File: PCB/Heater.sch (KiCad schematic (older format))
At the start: 29 parts, among them IC1 ATTINY45-P, P1 220V 50Hz, P2 ICP, P3 DS18B20, T1 SCR

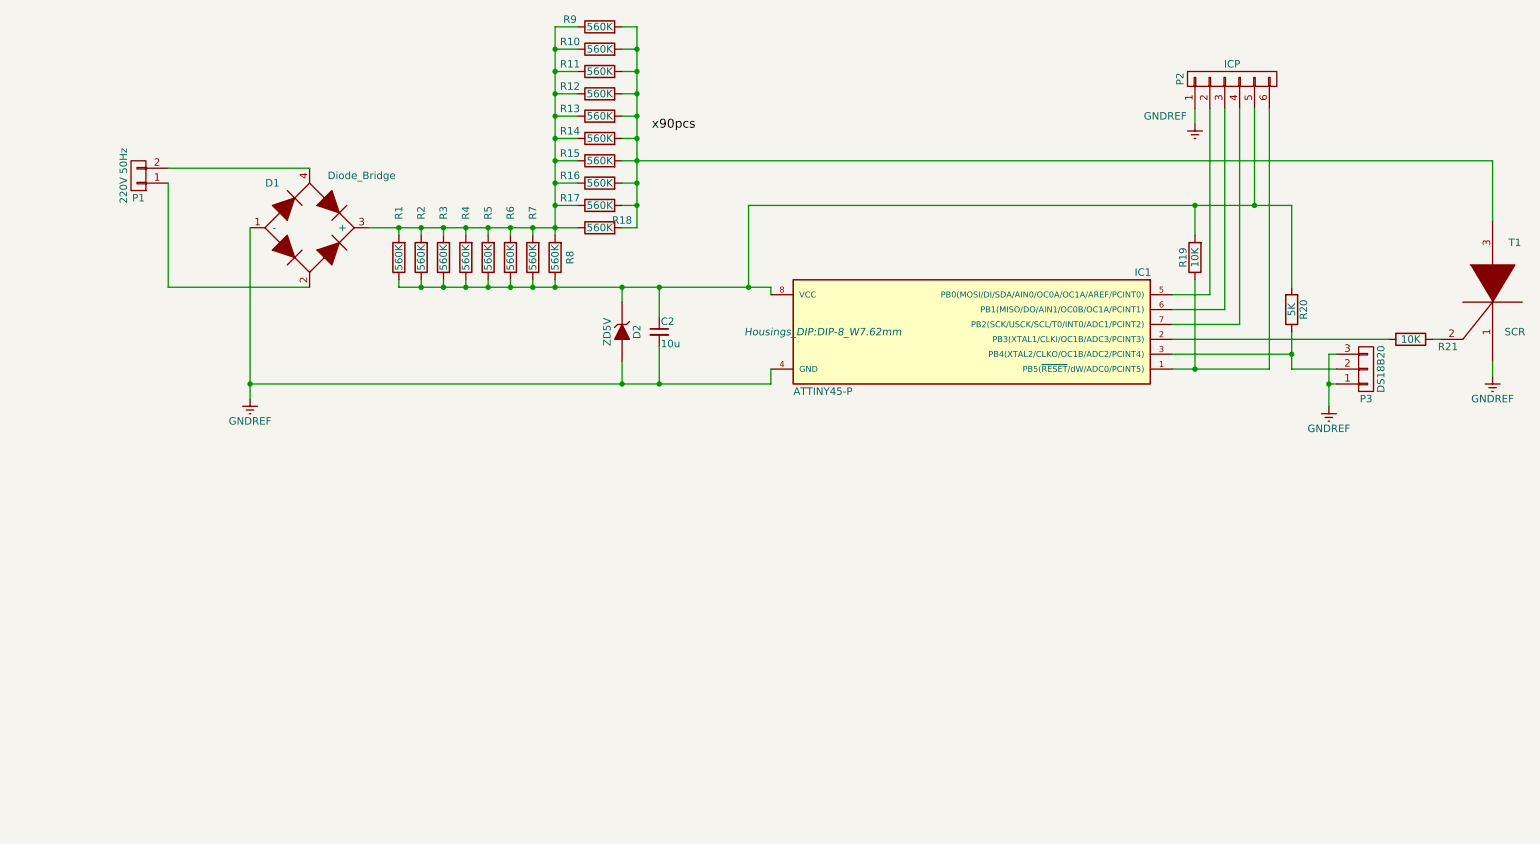
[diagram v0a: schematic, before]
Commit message: Updated Schematic and PCB to use optotriac
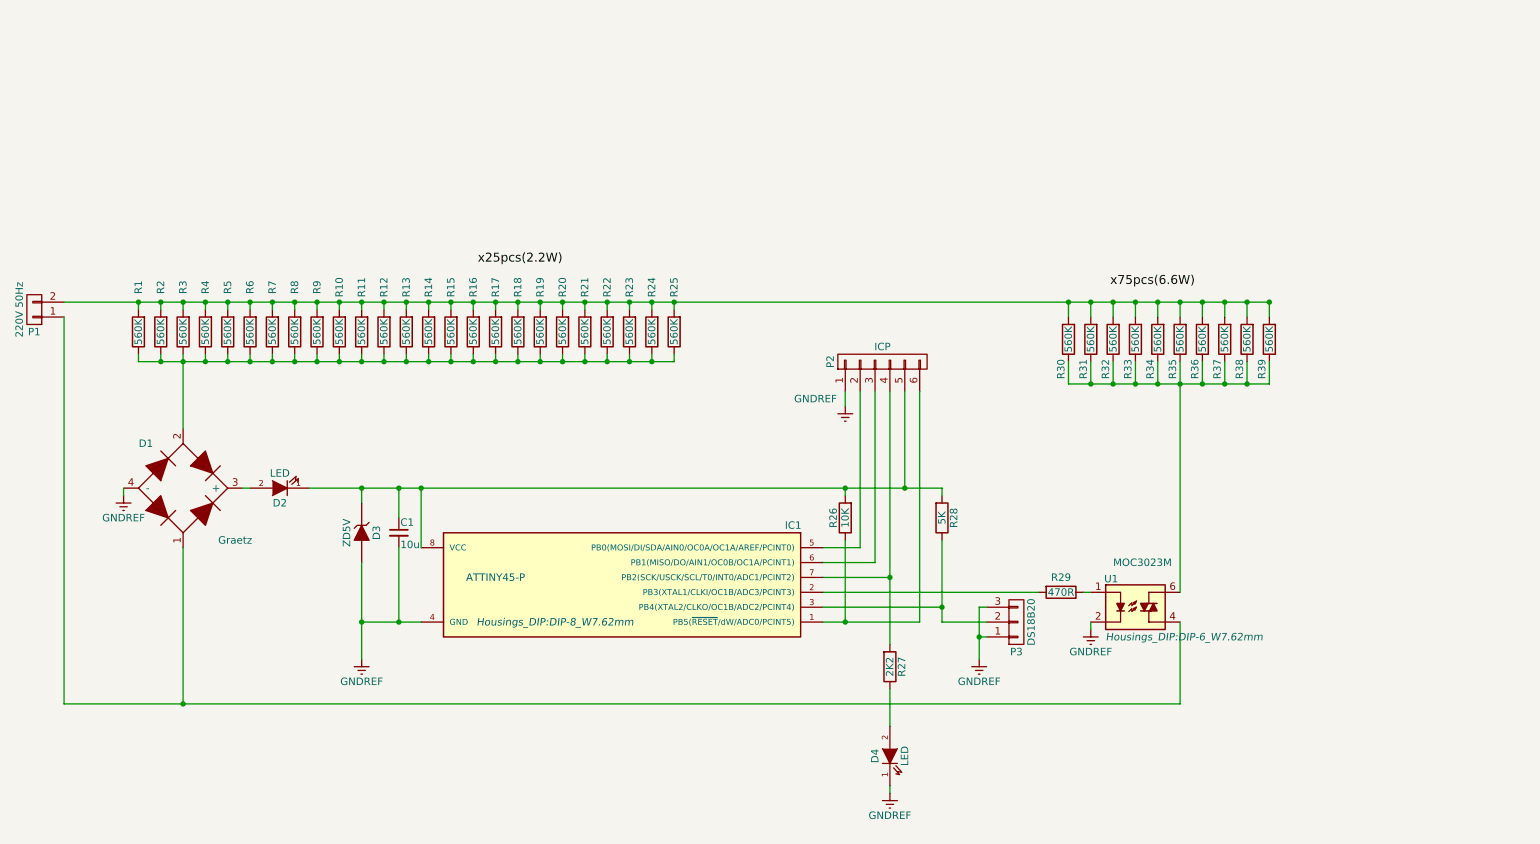
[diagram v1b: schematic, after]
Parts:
- removed D1: Diode_Bridge, Diodes_SMD:Diode_Bridge_TO-269AA, symbol Diode_Bridge
- removed T1: SCR, TO_SOT_Packages_THT:TO-92_Inline_Wide, symbol SCR
- added D1: Graetz, diodebridge:DIP-6_W7.62mm, symbol Graetz
- added D2, D4: LED, Socket_Strips:Socket_Strip_Straight_1x02_Pitch2.54mm, symbol LED
- added R10, R11, R12, R13, R14, R15, R16, R17, R18, R19, R20, R21, R22, R23, R24, R25, R9: 560K, Resistors_SMD:R_0805, symbol R
- added R27: 2K2, Resistors_SMD:R_0805, symbol R
- added U1: MOC3023M, Housings_DIP:DIP-6_W7.62mm, symbol MOC3023M
- R29: renamed from R21; value 10K -> 470R
- renumbered C2 to C1, D2 to D3, R19 to R26, R20 to R28, R9 to R30, R10 to R31, R11 to R32, R12 to R33, R13 to R34, R14 to R35, R15 to R36, R16 to R37, R17 to R38, R18 to R39
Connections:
- net GNDREF: now also D1.4 (-), D4.1 (K), U1.2
- net at IC1.7 (PB2(SCK/USCK/SCL/T0/INT0/ADC1/PCINT2)), P2.4 (P4): now also R27.2
- net at R1.1, R2.1, R3.1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: now also D1.2, R10.1, R11.1, R12.1, R13.1, R14.1, R15.1, R16.1, R17.1, R18.1, R19.1, R20.1, R21.1, R22.1, R23.1, R24.1, R25.1, R9.1; no longer C1.1, D3.1 (K), IC1.8 (VCC), P2.5 (P5), R26.2, R28.2
- net at R30.1, R31.1, R32.1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: now also U1.6; no longer R1.2, R2.2, R3.2, R4.2, R5.2, R6.2, R7.2, R8.2
- net at R29.1: now also U1.1
- net at P1.1 (P1): now also D1.1, U1.4
- net at P1.2 (P2): now also R1.2, R2.2, R3.2, R30.2, R31.2, R32.2, R33.2, R34.2, R35.2, R36.2, R37.2, R38.2, R39.2, R4.2, R5.2, R6.2, R7.2, R8.2, R10.2, R11.2, R12.2, R13.2, R14.2, R15.2, R16.2, R17.2, R18.2, R19.2, R20.2, R21.2, R22.2, R23.2, R24.2, R25.2, R9.2
- new net: C1.1, D2.1 (K), D3.1 (K), IC1.8 (VCC), P2.5 (P5), R26.2, R28.2
- new net: D1.3 (+), D2.2 (A)
- new net: D4.2 (A), R27.1
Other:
- moved on the sheet: C1, D3, IC1, P1, P2, P3, R1, R2, R26, R28, R29, R3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

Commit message: Added fw
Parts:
- D1: footprint diodebridge:DIP-6_W7.62mm -> Diodes_SMD:Diode_Bridge_TO-269AA
- D3: footprint Diodes_SMD:D_MELF -> Diodes_SMD:D_MELF_Handsoldering
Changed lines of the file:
@@
 LIBS:valves
 LIBS:diodebridge
+LIBS:Heater-cache
 EELAYER 25 0
 EELAYER END
@@
 F 0 "D3" H 3150 5150 50  0000 C CNN
 F 1 "ZD5V" H 3150 4950 50  0000 C CNN
-F 2 "Diodes_SMD:D_MELF" H 3150 5050 50  0001 C CNN
+F 2 "Diodes_SMD:D_MELF_Handsoldering" H 3150 5050 50  0001 C CNN
 F 3 "" H 3150 5050 50  0000 C CNN
 	1    3150 5050
@@
 F 0 "D1" H 1700 5050 50  0000 C CNN
 F 1 "Graetz" H 2300 4400 50  0000 C CNN
-F 2 "diodebridge:DIP-6_W7.62mm" H 1950 4750 50  0001 C CNN
+F 2 "Diodes_SMD:Diode_Bridge_TO-269AA" H 1950 4750 50  0001 C CNN
 F 3 "" H 1950 4750 50  0000 C CNN
 	1    1950 4750

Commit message: Not working yet
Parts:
- D2, D4: symbol LED -> LED-RESCUE-Heater
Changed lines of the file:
@@
 EESchema Schematic File Version 2
+LIBS:Heater-rescue
 LIBS:power
 LIBS:device
@@
 Connection ~ 1950 6200
 $Comp
-L LED D2
+L LED-RESCUE-Heater D2
 U 1 1 5961854B
 P 2600 4750
@@
 x25pcs(2.2W)
 $Comp
-L LED D4
+L LED-RESCUE-Heater D4
 U 1 1 5961C8F6
 P 6700 6550

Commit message: finished working version of the PCB and FW
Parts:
- removed P2: ICP, Socket_Strips:Socket_Strip_Straight_1x06_Pitch2.54mm, symbol CONN_01X06
- added J1: GND, Pin_Headers:Pin_Header_Straight_1x01_Pitch1.27mm, symbol CONN_01X01
- added J2: RST, Pin_Headers:Pin_Header_Straight_1x01_Pitch1.27mm, symbol CONN_01X01
- added P2: CONN_01X04, Pin_Headers:Pin_Header_Straight_1x04_Pitch2.54mm, symbol CONN_01X04
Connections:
- net GNDREF: now also J1.1 (P1)
- net at IC1.1 (PB5(~RESET~/dW/ADC0/PCINT5)), R26.1: now also J2.1 (P1)
- net at IC1.2 (PB3(XTAL1/CLKI/OC1B/ADC3/PCINT3)): now also P3.2 (P2), R28.1; no longer R29.2
- net at IC1.5 (PB0(MOSI/DI/SDA/AIN0/OC0A/OC1A/AREF/PCINT0)): now also P2.1 (P1)
- net at IC1.6 (PB1(MISO/DO/AIN1/OC0B/OC1A/PCINT1)): now also P2.2 (P2)
- net at IC1.7 (PB2(SCK/USCK/SCL/T0/INT0/ADC1/PCINT2)), R27.2: now also P2.3 (P3)
- net at C1.1, D2.1 (K), D3.1 (K)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: now also P2.4 (P4)
- net at D1.1, P1.1 (P1): now also U1.6; no longer U1.4
- net at R30.1, R31.1, R32.1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: now also U1.4; no longer U1.6
- new net: IC1.3 (PB4(XTAL2/CLKO/OC1B/ADC2/PCINT4)), R29.2
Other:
- moved on the sheet: P3, R29, U1
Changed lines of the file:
@@
 L CONN_01X03 P3
 U 1 1 595689AB
-P 7550 5650
-F 0 "P3" H 7550 5850 50  0000 C CNN
-F 1 "DS18B20" V 7650 5650 50  0000 C CNN
-F 2 "TO_SOT_Packages_THT:TO-92_Inline_Wide" H 7550 5650 50  0001 C CNN
-F 3 "" H 7550 5650 50  0000 C CNN
-	1    7550 5650
-	1    0    0    1
+P 7450 4800
+F 0 "P3" H 7450 5000 50  0000 C CNN
+F 1 "DS18B20" V 7550 4800 50  0000 C CNN
+F 2 "TO_SOT_Packages_THT:TO-92_Inline_Wide" H 7450 4800 50  0001 C CNN
+F 3 "" H 7450 4800 50  0000 C CNN
+	1    7450 4800
+	0    1    -1   0
 $EndComp
 $Comp
@@
 L R R29
 U 1 1 59568C3A
-P 7850 5450
-F 0 "R29" V 7750 5450 50  0000 C CNN
-F 1 "470R" V 7850 5450 50  0000 C CNN
-F 2 "Resistors_SMD:R_0805" V 7780 5450 50  0001 C CNN
-F 3 "" H 7850 5450 50  0000 C CNN
-	1    7850 5450
-	0    1    1    0
+P 8500 5550
+F 0 "R29" V 8400 5550 50  0000 C CNN
+F 1 "470R" V 8500 5550 50  0000 C CNN
+F 2 "Resistors_SMD:R_0805" V 8430 5550 50  0001 C CNN
+F 3 "" H 8500 5550 50  0000 C CNN
+	1    8500 5550
+	0    1    -1   0
 $EndComp
 $Comp
@@
 L GNDREF #PWR01
 U 1 1 5956A06F
-P 7300 5900
-F 0 "#PWR01" H 7300 5650 50  0001 C CNN
-F 1 "GNDREF" H 7300 5750 50  0000 C CNN
-F 2 "" H 7300 5900 50  0000 C CNN
-F 3 "" H 7300 5900 50  0000 C CNN
-	1    7300 5900
+P 7550 5150
+F 0 "#PWR01" H 7550 4900 50  0001 C CNN
+F 1 "GNDREF" H 7350 5100 50  0000 C CNN
+F 2 "" H 7550 5150 50  0000 C CNN
+F 3 "" H 7550 5150 50  0000 C CNN
+	1    7550 5150
 	-1   0    0    -1
 $EndComp
@@
 $EndComp
 $Comp
-L CONN_01X06 P2
-U 1 1 5956ABD8
-P 6650 3900
-F 0 "P2" H 6650 4250 50  0000 C CNN
-F 1 "ICP" V 6750 3900 50  0000 C CNN
-F 2 "Socket_Strips:Socket_Strip_Straight_1x06_Pitch2.54mm" H 6650 3900 50  0001 C CNN
-F 3 "" H 6650 3900 50  0000 C CNN
-	1    6650 3900
-	0    -1   -1   0
-$EndComp
-$Comp
 L R R5
 U 1 1 59576662
@@
 $Comp
 L GNDREF #PWR03
-U 1 1 5957BFE8
-P 6400 4200
-F 0 "#PWR03" H 6400 3950 50  0001 C CNN
-F 1 "GNDREF" H 6200 4250 50  0000 C CNN
-F 2 "" H 6400 4200 50  0000 C CNN
-F 3 "" H 6400 4200 50  0000 C CNN
-	1    6400 4200
-	1    0    0    -1
-$EndComp
-$Comp
-L GNDREF #PWR04
 U 1 1 59613334
 P 3150 5900
-F 0 "#PWR04" H 3150 5650 50  0001 C CNN
+F 0 "#PWR03" H 3150 5650 50  0001 C CNN
 F 1 "GNDREF" H 3150 5750 50  0000 C CNN
 F 2 "" H 3150 5900 50  0000 C CNN
@@
 L MOC3023M U1
 U 1 1 59614FA8
-P 8350 5550
-F 0 "U1" H 8140 5740 50  0000 L CNN
-F 1 "MOC3023M" H 8200 5850 50  0000 L CNN
-F 2 "Housings_DIP:DIP-6_W7.62mm" H 8150 5350 50  0000 L CIN
-F 3 "" H 8325 5550 50  0000 L CNN
-	1    8350 5550
-	1    0    0    -1
+P 8750 5900
+F 0 "U1" H 8540 6090 50  0000 L CNN
+F 1 "MOC3023M" H 8600 6200 50  0000 L CNN
+F 2 "Housings_DIP:DIP-6_W7.62mm" H 8550 5700 50  0000 L CIN
+F 3 "" H 8725 5900 50  0000 L CNN
+	1    8750 5900
+	0    -1   1    0
 $EndComp
 Connection ~ 2700 3900
@@
 Wire Wire Line
 	6250 5650 6900 5650
-Wire Wire Line
-	6250 5450 7700 5450
 Wire Wire Line
 	1650 3550 1650 3500
@@
 	3400 4950 3400 4750
 Connection ~ 3400 4750
-Wire Wire Line
-	8000 5450 8050 5450
 Connection ~ 6400 5650
 Wire Wire Line
@@
 	8800 3900 8800 4050
 Connection ~ 8800 4050
-Wire Wire Line
-	8650 3900 8650 5450
 Connection ~ 8650 4050
 Wire Wire Line
@@
 Wire Wire Line
 	9250 3500 9250 3600
-Wire Wire Line
-	6400 4200 6400 4100
 Connection ~ 6400 4750
 Connection ~ 6800 4750
 Wire Wire Line
-	6250 5550 7050 5550
-Wire Wire Line
-	7050 5100 7050 5650
-Wire Wire Line
-	7050 5650 7350 5650
-Wire Wire Line
-	7300 5750 7350 5750
-Wire Wire Line
-	7300 5550 7350 5550
-Connection ~ 7300 5750
-Wire Wire Line
-	7300 5550 7300 5900
-Connection ~ 7050 5550
+	7450 5000 7450 5450
+Wire Wire Line
+	7550 5000 7550 5150
+Wire Wire Line
+	7350 5050 7350 5000
+Connection ~ 7550 5050
 Wire Wire Line
 	2800 4750 7050 4750
@@
 Wire Wire Line
 	6800 4750 6800 4100
-Wire Wire Line
-	6900 5650 6900 4100
 Wire Wire Line
 	7050 4750 7050 4800
@@
 Connection ~ 3400 5650
 $Comp
-L GNDREF #PWR05
+L GNDREF #PWR04
 U 1 1 5961517B
-P 8050 5700
-F 0 "#PWR05" H 8050 5450 50  0001 C CNN
-F 1 "GNDREF" H 8050 5550 50  0000 C CNN
-F 2 "" H 8050 5700 50  0000 C CNN
-F 3 "" H 8050 5700 50  0000 C CNN
-	1    8050 5700
-	-1   0    0    -1
-$EndComp
-Wire Wire Line
-	8050 5700 8050 5650
+P 9050 5550
+F 0 "#PWR04" H 9050 5300 50  0001 C CNN
+F 1 "GNDREF" V 9100 5700 50  0000 C CNN
+F 2 "" H 9050 5550 50  0000 C CNN
+F 3 "" H 9050 5550 50  0000 C CNN
+	1    9050 5550
+	0    -1   -1   0
+$EndComp
 Wire Wire Line
 	1150 6200 8650 6200
 Wire Wire Line
-	8650 6200 8650 5650
-Wire Wire Line
-	9250 3900 9250 4050
+	9250 3900 9250 6200
 Wire Wire Line
 	9250 4050 7900 4050
@@
 $EndComp
 $Comp
-L GNDREF #PWR06
+L GNDREF #PWR05
 U 1 1 5961CE30
 P 6700 6800
-F 0 "#PWR06" H 6700 6550 50  0001 C CNN
+F 0 "#PWR05" H 6700 6550 50  0001 C CNN
 F 1 "GNDREF" H 6700 6650 50  0000 C CNN
 F 2 "" H 6700 6800 50  0000 C CNN
@@
 	1    0    0    -1
 $EndComp
+Wire Wire Line
+	7450 5450 6250 5450
+Wire Wire Line
+	7350 5050 7550 5050
+Wire Wire Line
+	7050 5100 7050 5450
+Connection ~ 7050 5450
+$Comp
+L CONN_01X04 P2
+U 1 1 59649114
+P 6650 3900
+F 0 "P2" H 6650 4150 50  0000 C CNN
+F 1 "CONN_01X04" V 6750 3900 50  0000 C CNN
+F 2 "Pin_Headers:Pin_Header_Straight_1x04_Pitch2.54mm" H 6650 3900 50  0001 C CNN
+F 3 "" H 6650 3900 50  0001 C CNN
+	1    6650 3900
+	0    -1   -1   0
+$EndComp
+$Comp
+L CONN_01X01 J2
+U 1 1 5964941A
+P 7100 5650
+F 0 "J2" H 7100 5750 50  0000 C CNN
+F 1 "RST" H 7250 5650 50  0000 C CNN
+F 2 "Pin_Headers:Pin_Header_Straight_1x01_Pitch1.27mm" H 7100 5650 50  0001 C CNN
+F 3 "" H 7100 5650 50  0001 C CNN
+	1    7100 5650
+	1    0    0    -1
+$EndComp
+$Comp
+L CONN_01X01 J1
+U 1 1 5964958B
+P 2950 5650
+F 0 "J1" H 2950 5750 50  0000 C CNN
+F 1 "GND" H 3100 5650 50  0000 C CNN
+F 2 "Pin_Headers:Pin_Header_Straight_1x01_Pitch1.27mm" H 2950 5650 50  0001 C CNN
+F 3 "" H 2950 5650 50  0001 C CNN
+	1    2950 5650
+	-1   0    0    1
+$EndComp
+Wire Wire Line
+	8650 3900 8650 4050
+Wire Wire Line
+	8650 5550 8650 5600
+Wire Wire Line
+	8350 5550 6250 5550
+Wire Wire Line
+	9050 5550 8850 5550
+Wire Wire Line
+	8850 5550 8850 5600
+Wire Wire Line
+	9250 6200 8850 6200
+Connection ~ 9250 4050
 $EndSCHEMATC

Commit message: A better packed version
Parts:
- removed D2: LED, Socket_Strips:Socket_Strip_Straight_1x02_Pitch2.54mm, symbol LED-RESCUE-Heater
- D1: footprint Diodes_SMD:Diode_Bridge_TO-269AA -> diodebridge:DIP-6_W7.62mm
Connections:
- net at P3.2 (P2), R28.1: now also IC1.7 (PB2(SCK/USCK/SCL/T0/INT0/ADC1/PCINT2)), P2.3 (P3); no longer IC1.2 (PB3(XTAL1/CLKI/OC1B/ADC3/PCINT3))
- net at IC1.5 (PB0(MOSI/DI/SDA/AIN0/OC0A/OC1A/AREF/PCINT0)), P2.1 (P1): now also R27.2
- net at C1.1, D3.1 (K), IC1.8 (VCC)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: now also D1.3 (+)
- net at R1.1, R10.1, R11.1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: now also D1.1; no longer D1.2
- net at R1.2, R10.2, R11.2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: now also P1.1 (P1); no longer P1.2 (P2)
- net at R30.1, R31.1, R32.1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: now also U1.6; no longer U1.4
- new net: D1.2, P1.2 (P2), U1.4
- no-connect marks 0 -> 1
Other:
- moved on the sheet: D4, R27, U1
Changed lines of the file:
@@
 F 3 "" H 950 3550 50  0000 C CNN
 	1    950  3550
-	-1   0    0    1
+	-1   0    0    -1
 $EndComp
 $Comp
@@
 L MOC3023M U1
 U 1 1 59614FA8
-P 8750 5900
-F 0 "U1" H 8540 6090 50  0000 L CNN
-F 1 "MOC3023M" H 8600 6200 50  0000 L CNN
-F 2 "Housings_DIP:DIP-6_W7.62mm" H 8550 5700 50  0000 L CIN
-F 3 "" H 8725 5900 50  0000 L CNN
-	1    8750 5900
-	0    -1   1    0
+P 8950 5800
+F 0 "U1" H 8740 5990 50  0000 L CNN
+F 1 "MOC3023M" H 8800 6100 50  0000 L CNN
+F 2 "Housings_DIP:DIP-6_W7.62mm" H 8750 5600 50  0000 L CIN
+F 3 "" H 8925 5800 50  0000 L CNN
+	1    8950 5800
+	1    0    0    -1
 $EndComp
 Connection ~ 2700 3900
-Wire Wire Line
-	6700 5350 6250 5350
 Wire Wire Line
 	6600 5250 6250 5250
@@
 Connection ~ 6800 4750
 Wire Wire Line
-	7450 5000 7450 5450
-Wire Wire Line
 	7550 5000 7550 5150
 Wire Wire Line
@@
 Connection ~ 7550 5050
 Wire Wire Line
-	2800 4750 7050 4750
+	2350 4750 7050 4750
 Wire Wire Line
 	1650 3850 1650 3900
@@
 	6400 5100 6400 5650
 Wire Wire Line
-	6500 5150 6500 4100
-Wire Wire Line
-	6600 4100 6600 5250
-Wire Wire Line
-	6700 4100 6700 5800
+	6500 4100 6500 5800
 Wire Wire Line
 	6800 4750 6800 4100
@@
 L GNDREF #PWR04
 U 1 1 5961517B
-P 9050 5550
-F 0 "#PWR04" H 9050 5300 50  0001 C CNN
-F 1 "GNDREF" V 9100 5700 50  0000 C CNN
-F 2 "" H 9050 5550 50  0000 C CNN
-F 3 "" H 9050 5550 50  0000 C CNN
-	1    9050 5550
-	0    -1   -1   0
-$EndComp
-Wire Wire Line
-	1150 6200 8650 6200
-Wire Wire Line
-	9250 3900 9250 6200
+P 8650 5950
+F 0 "#PWR04" H 8650 5700 50  0001 C CNN
+F 1 "GNDREF" H 8400 5900 50  0000 C CNN
+F 2 "" H 8650 5950 50  0000 C CNN
+F 3 "" H 8650 5950 50  0000 C CNN
+	1    8650 5950
+	1    0    0    -1
+$EndComp
+Wire Wire Line
+	1150 6200 9250 6200
 Wire Wire Line
 	9250 4050 7900 4050
@@
 	1950 5150 1950 6200
 Connection ~ 1950 6200
-$Comp
-L LED-RESCUE-Heater D2
-U 1 1 5961854B
-P 2600 4750
-F 0 "D2" H 2600 4850 50  0000 C CNN
-F 1 "LED" H 2600 4650 50  0000 C CNN
-F 2 "Socket_Strips:Socket_Strip_Straight_1x02_Pitch2.54mm" H 2600 4750 50  0001 C CNN
-F 3 "" H 2600 4750 50  0000 C CNN
-	1    2600 4750
-	-1   0    0    1
-$EndComp
-Wire Wire Line
-	2400 4750 2350 4750
 Wire Wire Line
 	2700 3900 2700 3850
@@
 L LED-RESCUE-Heater D4
 U 1 1 5961C8F6
-P 6700 6550
-F 0 "D4" H 6700 6650 50  0000 C CNN
-F 1 "LED" H 6700 6450 50  0000 C CNN
-F 2 "Socket_Strips:Socket_Strip_Straight_1x02_Pitch2.54mm" H 6700 6550 50  0001 C CNN
-F 3 "" H 6700 6550 50  0000 C CNN
-	1    6700 6550
+P 6500 6450
+F 0 "D4" H 6500 6550 50  0000 C CNN
+F 1 "LED" H 6500 6350 50  0000 C CNN
+F 2 "Socket_Strips:Socket_Strip_Straight_1x02_Pitch2.54mm" H 6500 6450 50  0001 C CNN
+F 3 "" H 6500 6450 50  0000 C CNN
+	1    6500 6450
 	0    -1   -1   0
 $EndComp
@@
 L GNDREF #PWR05
 U 1 1 5961CE30
-P 6700 6800
-F 0 "#PWR05" H 6700 6550 50  0001 C CNN
-F 1 "GNDREF" H 6700 6650 50  0000 C CNN
-F 2 "" H 6700 6800 50  0000 C CNN
-F 3 "" H 6700 6800 50  0000 C CNN
-	1    6700 6800
+P 6500 6700
+F 0 "#PWR05" H 6500 6450 50  0001 C CNN
+F 1 "GNDREF" H 6500 6550 50  0000 C CNN
+F 2 "" H 6500 6700 50  0000 C CNN
+F 3 "" H 6500 6700 50  0000 C CNN
+	1    6500 6700
 	-1   0    0    -1
 $EndComp
 Wire Wire Line
-	6700 6800 6700 6750
+	6500 6700 6500 6650
 $Comp
 L R R27
 U 1 1 5961D0D6
-P 6700 5950
-F 0 "R27" V 6780 5950 50  0000 C CNN
-F 1 "2K2" V 6700 5950 50  0000 C CNN
-F 2 "Resistors_SMD:R_0805" V 6630 5950 50  0001 C CNN
-F 3 "" H 6700 5950 50  0000 C CNN
-	1    6700 5950
+P 6500 5950
+F 0 "R27" V 6580 5950 50  0000 C CNN
+F 1 "2K2" V 6500 5950 50  0000 C CNN
+F 2 "Resistors_SMD:R_0805" V 6430 5950 50  0001 C CNN
+F 3 "" H 6500 5950 50  0000 C CNN
+	1    6500 5950
 	1    0    0    1
 $EndComp
-Wire Wire Line
-	6700 6100 6700 6350
-Connection ~ 6700 5350
 $Comp
 L Graetz D1
@@
 F 0 "D1" H 1700 5050 50  0000 C CNN
 F 1 "Graetz" H 2300 4400 50  0000 C CNN
-F 2 "Diodes_SMD:Diode_Bridge_TO-269AA" H 1950 4750 50  0001 C CNN
+F 2 "diodebridge:DIP-6_W7.62mm" H 1950 4750 50  0001 C CNN
 F 3 "" H 1950 4750 50  0000 C CNN
 	1    1950 4750
-	1    0    0    -1
-$EndComp
-Wire Wire Line
-	7450 5450 6250 5450
+	1    0    0    1
+$EndComp
 Wire Wire Line
 	7350 5050 7550 5050
-Wire Wire Line
-	7050 5100 7050 5450
-Connection ~ 7050 5450
 $Comp
 L CONN_01X04 P2
@@
 	8650 3900 8650 4050
 Wire Wire Line
-	8650 5550 8650 5600
+	8650 5550 8650 5700
 Wire Wire Line
 	8350 5550 6250 5550
-Wire Wire Line
-	9050 5550 8850 5550
-Wire Wire Line
-	8850 5550 8850 5600
-Wire Wire Line
-	9250 6200 8850 6200
 Connection ~ 9250 4050
+Wire Wire Line
+	8650 5950 8650 5900
+Wire Wire Line
+	9250 6200 9250 5900
+Wire Wire Line
+	9250 5700 9250 3900
+Wire Wire Line
+	6250 5350 7450 5350
+Wire Wire Line
+	7050 5350 7050 5100
+Wire Wire Line
+	7450 5350 7450 5000
+Connection ~ 7050 5350
+Wire Wire Line
+	6700 4100 6700 5350
+Connection ~ 6700 5350
+NoConn ~ 6250 5450
+Wire Wire Line
+	6600 5250 6600 4100
+Connection ~ 6500 5150
+Wire Wire Line
+	6500 6100 6500 6250
 $EndSCHEMATC
